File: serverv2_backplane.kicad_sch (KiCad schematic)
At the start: 49 parts, among them J1 Conn_02x12_Counter_Clockwise, U1 RTL9210B-CG, U2 W25Q128JVSIQTR, U3 ETA3521FSG_C22362743, X1 X322525MOB4SI

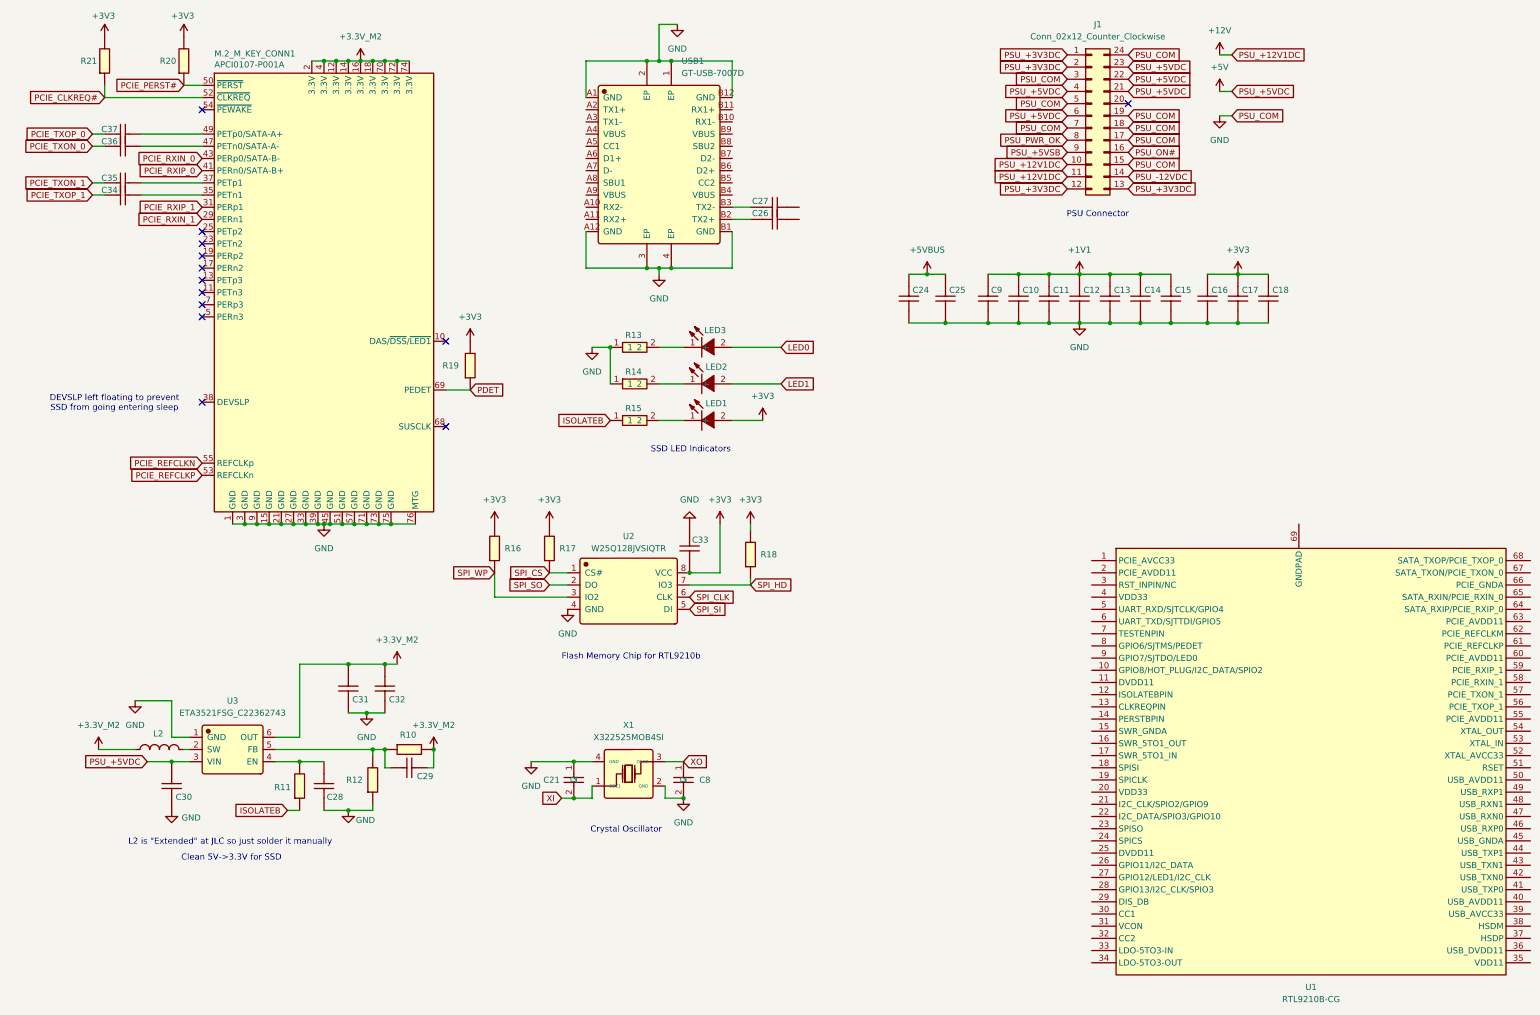
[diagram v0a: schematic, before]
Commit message: Made preliminary TUSB1064 schematic
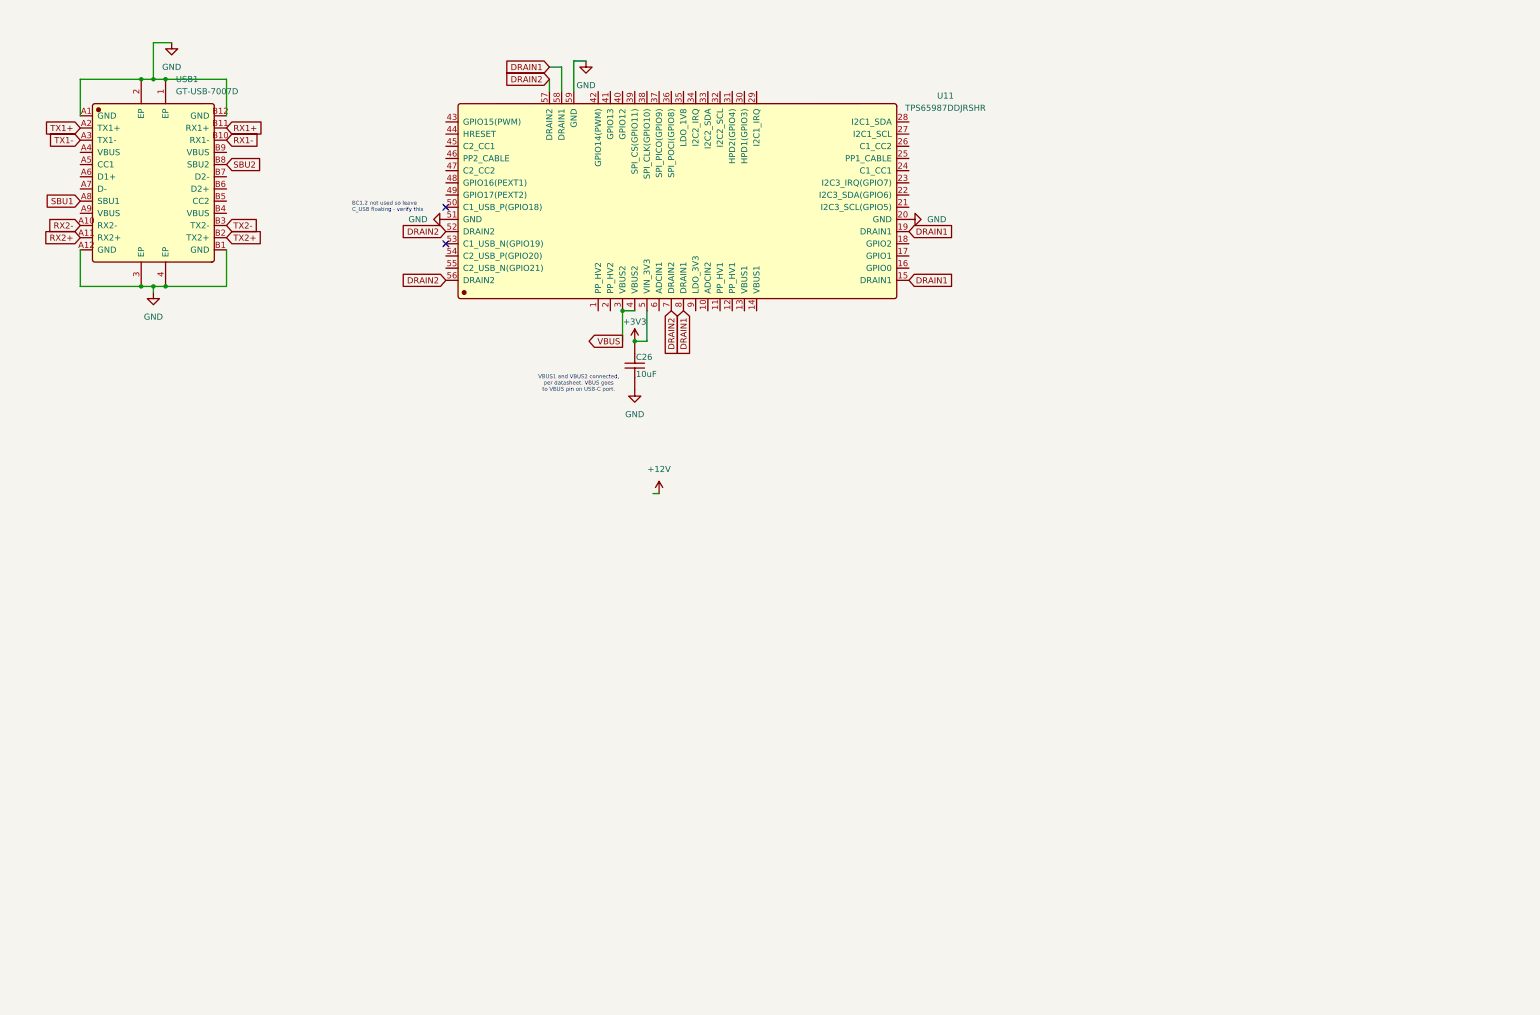
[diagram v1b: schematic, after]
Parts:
- removed C10, C11, C12, C13, C14, C15, C16, C17, C18, C26, C27, C28, C9: CL05B104KB54PNC, Capacitor_SMD:C_0402_1005Metric, symbol JLCImport:CL05B104KB54PNC
- removed C21, C8: 0402CG150J500NT, Capacitor_SMD:C_0402_1005Metric, symbol JLCImport:0402CG150J500NT
- removed C24, C25: CL10A106KP8NNNC, Capacitor_SMD:C_0603_1608Metric, symbol JLCImport:CL10A106KP8NNNC
- removed C29: 0402CG470J500NT, Capacitor_SMD:C_0402_1005Metric, symbol JLCImport:0402CG470J500NT
- removed C30, C31, C32: CL10A226MQ8NRNC, Capacitor_SMD:C_0603_1608Metric, symbol JLCImport:CL10A226MQ8NRNC
- removed C33: CL10A105KB8NNNC, Capacitor_SMD:C_0603_1608Metric, symbol JLCImport:CL10A105KB8NNNC
- removed C34, C35, C36, C37: CL05B224KO5NNNC, Capacitor_SMD:C_0402_1005Metric, symbol JLCImport:CL05B224KO5NNNC
- removed J1: Conn_02x12_Counter_Clockwise, Connector_Molex:Molex_Mini-Fit_Jr_5566-24A_2x12_P4.20mm_Vertical, symbol Connector_Generic:Conn_02x12_Counter_Clockwise
- removed L2: FTC252012S1R0MBCA, TerminalBlock_Phoenix:TerminalBlock_Phoenix_PTSM-0,5-2-2,5-V-SMD_1x02-1MP_P2.50mm_Vertical, symbol JLCImport:FTC252012S1R0MBCA
- removed LED1, LED2, LED3: FC-2012HRK-620D, JLCImport:FC-2012HRK-620D, symbol JLCImport:FC-2012HRK-620D
- removed M.2_M_KEY_CONN1: APCI0107-P001A, JLCImport:APCI0107-P001A, symbol Connector:Bus_M.2_Socket_M
- removed R10: 0603WAF6802T5E, Resistor_SMD:R_0603_1608Metric, symbol JLCImport:0603WAF6802T5E
- removed R11, R19: 0402WGF1003TCE, Resistor_SMD:R_0402_1005Metric, symbol JLCImport:0402WGF1003TCE
- removed R12: 0402WGF1502TCE, Resistor_SMD:R_0402_1005Metric, symbol JLCImport:0402WGF1502TCE
- removed R13, R14, R15: 0603WAF2200T5E, Resistor_SMD:R_0603_1608Metric, symbol JLCImport:0603WAF2200T5E
- removed R16, R17, R18, R20, R21: 0402WGF1002TCE, Resistor_SMD:R_0402_1005Metric, symbol JLCImport:0402WGF1002TCE
- removed U1: RTL9210B-CG, RTL9210B-CG:QFN-68_L8.0-W8.0-P0.40-BL-EP4.8, symbol RTL9210B-CG:RTL9210B-CG
- removed U2: W25Q128JVSIQTR, Package_SO:SOIC-8_5.3x5.3mm_P1.27mm, symbol JLCImport:W25Q128JVSIQTR
- removed U3: ETA3521FSG_C22362743, Package_TO_SOT_SMD:SOT-563, symbol JLCImport:ETA3521FSG_C22362743
- removed X1: X322525MOB4SI, Crystal:Crystal_SMD_3225-4Pin_3.2x2.5mm, symbol JLCImport:X322525MOB4SI
- added C26: 10uF, Capacitor_SMD:C_0603_1608Metric, symbol JLCImport:CL10A106KP8NNNC
- added U11: TPS65987DDJRSHR, JLCImport:TPS65987DDJRSHR, symbol JLCImport:TPS65987DDJRSHR
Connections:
- net +3V3: now also C26.2, U11.5 (VIN_3V3)
- net GND: now also C26.1, U11.20 (GND), U11.51 (GND), U11.59 (GND)
- net TX2-: now reaches USB1.B3 (TX2-)
- net RX2-: now reaches USB1.A10 (RX2-)
- net RX2+: now reaches USB1.A11 (RX2+)
- net TX1+: now reaches USB1.A2 (TX1+)
- net TX1-: now reaches USB1.A3 (TX1-)
- net SBU1: now reaches USB1.A8 (SBU1)
- net RX1-: now reaches USB1.B10 (RX1-)
- net RX1+: now reaches USB1.B11 (RX1+)
- net TX2+: now reaches USB1.B2 (TX2+)
- net SBU2: now reaches USB1.B8 (SBU2)
- new net DRAIN1: U11.15 (DRAIN1), U11.19 (DRAIN1), U11.58 (DRAIN1), U11.8 (DRAIN1)
- new net DRAIN2: U11.52 (DRAIN2), U11.56 (DRAIN2), U11.57 (DRAIN2), U11.7 (DRAIN2)
- new net VBUS: U11.3 (VBUS2), U11.4 (VBUS2)
- no-connect marks 13 -> 2
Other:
- note added: "BC1.2 not used so leave C_USB floating - verify this"
- note added: "VBUS1 and VBUS2 connected, per datasheet. VBUS goes to VBUS pin on USB-C port."
- note removed: "Clean 5V->3.3V for SSD"
- note removed: "Crystal Oscillator"
- note removed: "DEVSLP left floating to prevent SSD from going entering sleep"
- note removed: "Flash Memory Chip for RTL9210b"
- note removed: "L2 is "Extended" at JLC so just solder it manually"
- note removed: "PSU Connector"
- note removed: "SSD LED Indicators"

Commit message: Preliminary Revision of PS176 DP->HDMI Subsystem
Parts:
- added CN3: H2541FV-C762-2X04P, JLCImport:H2541FV-C762-2X04P, symbol JLCImport:H2541FV-C762-2X04P
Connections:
- net CTRL_SCL: now reaches U11.21 (I2C3_SCL(GPIO5))
- net CTRL_SDA: now reaches U11.22 (I2C3_SDA(GPIO6))
- net CTRL_LDO_3V3: now reaches U11.9 (LDO_3V3)
- no-connect marks 2 -> 3
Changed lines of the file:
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@@
+	)
+	(no_connect
+		(at 201.93 48.26)
 	)
 	(no_connect
@@
 	(wire
 		(pts
+			(xy 157.48 93.98) (xy 157.48 74.93)
+		)
+		(stroke
+			(width 0)
+			(type default)
+		)
+	)
+	(wire
+		(pts
+			(xy 152.4 93.98) (xy 157.48 93.98)
+		)
+		(stroke
+			(width 0)
+			(type default)
+		)
+	)
+	(wire
+		(pts
 			(xy 41.91 26.67) (xy 44.45 26.67)
 		)
@@
 		(pts
 			(xy 59.69 26.67) (xy 59.69 34.29)
-		)
-		(stroke
-			(width 0)
-			(type default)
-		)
-	)
-	(wire
-		(pts
-			(xy 149.86 113.03) (xy 148.59 113.03)
 		)
 		(stroke
@@
 		)
 	)
+	(global_label "CTRL_SDA"
+		(shape input)
+		(at 201.93 50.8 0)
+		(fields_autoplaced yes)
+		(effects
+			(font
+				(size 1.27 1.27)
+			)
+			(justify left)
+		)
+		(property "Intersheetrefs" "${INTERSHEET_REFS}"
+			(at 213.9866 50.8 0)
+			(hide yes)
+			(show_name no)
+			(do_not_autoplace no)
+			(effects
+				(font
+					(size 1.27 1.27)
+				)
+				(justify left)
+			)
+		)
+	)
 	(global_label "DRAIN1"
 		(shape input)
@@
 				)
 				(justify right)
+			)
+		)
+	)
+	(global_label "CTRL_SCL"
+		(shape input)
+		(at 201.93 53.34 0)
+		(fields_autoplaced yes)
+		(effects
+			(font
+				(size 1.27 1.27)
+			)
+			(justify left)
+		)
+		(property "Intersheetrefs" "${INTERSHEET_REFS}"
+			(at 213.9261 53.34 0)
+			(hide yes)
+			(show_name no)
+			(do_not_autoplace no)
+			(effects
+				(font
+					(size 1.27 1.27)
+				)
+				(justify left)
 			)
 		)
@@
 	)
 	(symbol
+		(lib_id "power:+3V3")
+		(at 152.4 93.98 0)
+		(unit 1)
+		(body_style 1)
+		(exclude_from_sim no)
+		(in_bom yes)
+		(on_board yes)
+		(in_pos_files yes)
+		(dnp no)
+		(property "Reference" "#PWR0164"
+			(at 152.4 97.79 0)
+			(hide yes)
+			(show_name no)
+			(do_not_autoplace no)
+			(effects
+				(font
+					(size 1.27 1.27)
+				)
+			)
+		)
+		(property "Value" "CTRL_LDO_3V3"
+			(at 147.828 90.17 0)
+			(show_name no)
+			(do_not_autoplace no)
+			(effects
+				(font
+					(size 0.8128 0.8128)
+				)
+				(justify left)
+			)
+		)
+		(property "Footprint" ""
+			(at 152.4 93.98 0)
+			(hide yes)
+			(show_name no)
+			(do_not_autoplace no)
+			(effects
+				(font
+					(size 1.27 1.27)
+				)
+			)
+		)
+		(property "Datasheet" ""
+			(at 152.4 93.98 0)
+			(hide yes)
+			(show_name no)
+			(do_not_autoplace no)
+			(effects
+				(font
+					(size 1.27 1.27)
+				)
+			)
+		)
+		(property "Description" "Power symbol creates a global label with name \"+3V3\""
+			(at 152.4 93.98 0)
+			(hide yes)
+			(show_name no)
+			(do_not_autoplace no)
+			(effects
+				(font
+					(size 1.27 1.27)
+				)
+			)
+		)
+		(pin "1"
+		)
+		(instances
+			(project "serverv2_backplane"
+				(path "/d38d6818-cf53-410d-afa3-a75a85b7c05a"
+					(reference "#PWR0164")
+					(unit 1)
+				)
+			)
+		)
+	)
+	(symbol
 		(lib_id "power:GND")
 		(at 134.62 22.86 0)
@@
 	)
 	(symbol
-		(lib_id "power:+5V")
-		(at 149.86 113.03 0)
+		(lib_id "JLCImport:H2541FV-C762-2X04P")
+		(at 217.17 90.17 0)
 		(unit 1)
 		(body_style 1)
@@
 		(dnp no)
 		(fields_autoplaced yes)
-		(property "Reference" "#PWR0144"
-			(at 149.86 116.84 0)
-			(hide yes)
-			(show_name no)
-			(do_not_autoplace no)
-			(effects
-				(font
-					(size 1.27 1.27)
-				)
-			)
-		)
-		(property "Value" "+12V"
-			(at 149.86 107.95 0)
-			(show_name no)
-			(do_not_autoplace no)
-			(effects
-				(font
-					(size 1.27 1.27)
-				)
-			)
-		)
-		(property "Footprint" ""
-			(at 149.86 113.03 0)
-			(hide yes)
-			(show_name no)
-			(do_not_autoplace no)
-			(effects
-				(font
-					(size 1.27 1.27)
-				)
-			)
-		)
-		(property "Datasheet" ""
-			(at 149.86 113.03 0)
-			(hide yes)
-			(show_name no)
-			(do_not_autoplace no)
-			(effects
-				(font
-					(size 1.27 1.27)
-				)
-			)
-		)
-		(property "Description" "Power symbol creates a global label with name \"+5V\""
-			(at 149.86 113.03 0)
-			(hide yes)
-			(show_name no)
-			(do_not_autoplace no)
-			(effects
-				(font
-					(size 1.27 1.27)
-				)
-			)
+		(property "Reference" "CN3"
+			(at 217.17 78.74 0)
+			(show_name no)
+			(do_not_autoplace no)
+			(effects
+				(font
+					(size 1.27 1.27)
+				)
+			)
+		)
+		(property "Value" "H2541FV-C762-2X04P"
+			(at 217.17 81.28 0)
+			(show_name no)
+			(do_not_autoplace no)
+			(effects
+				(font
+					(size 1.27 1.27)
+				)
+			)
+		)
+		(property "Footprint" "JLCImport:H2541FV-C762-2X04P"
+			(at 217.17 90.17 0)
+			(hide yes)
+			(show_name no)
+			(do_not_autoplace no)
+			(effects
+				(font
+					(size 1.27 1.27)
+				)
+			)
+		)
+		(property "Datasheet" "https://www.lcsc.com/datasheet/lcsc_datasheet_2405141422_HanElectricity-H2541FV-C762-2x04P_C22387106.pdf"
+			(at 217.17 90.17 0)
+			(hide yes)
+			(show_name no)
+			(do_not_autoplace no)
+			(effects
+				(font
+					(size 1.27 1.27)
+				)
+			)
+		)
+		(property "Description" "-55℃~+105℃ 2.54mm 7.62mm 8P DIP Phosphor bronze Square Hole DIP-8 IC / Transistor Socket ROHS"
+			(at 217.17 90.17 0)
+			(hide yes)
+			(show_name no)
+			(do_not_autoplace no)
+			(effects
+				(font
+					(size 1.27 1.27)
+				)
+			)
+		)
+		(property "LCSC" "C22387106"
+			(at 217.17 90.17 0)
+			(hide yes)
+			(show_name no)
+			(do_not_autoplace no)
+			(effects
+				(font
+					(size 1.27 1.27)
+				)
+			)
+		)
+		(property "Manufacturer" "HanElectricity"
+			(at 217.17 90.17 0)
+			(hide yes)
+			(show_name no)
+			(do_not_autoplace no)
+			(effects
+				(font
+					(size 1.27 1.27)
+				)
+			)
+		)
+		(property "Manufacturer Part" "H2541FV-C762-2x04P"
+			(at 217.17 90.17 0)
+			(hide yes)
+			(show_name no)
+			(do_not_autoplace no)
+			(effects
+				(font
+					(size 1.27 1.27)
+				)
+			)
+		)
+		(pin "2"
 		)
 		(pin "1"
+		)
+		(pin "8"
+		)
+		(pin "3"
+		)
+		(pin "5"
+		)
+		(pin "7"
+		)
+		(pin "4"
+		)
+		(pin "6"
 		)
 		(instances
 			(project "serverv2_backplane"
 				(path "/d38d6818-cf53-410d-afa3-a75a85b7c05a"
-					(reference "#PWR0144")
+					(reference "CN3")
 					(unit 1)
 				)
